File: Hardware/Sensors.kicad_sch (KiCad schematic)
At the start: 8 parts, among them U11 DPS368, U7 BU27006MUC-ZTR

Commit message: Mega commit
Post review changes
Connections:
- net CSB renamed CS_Baro
- net SDI renamed SDI_Baro
- net SDO renamed SDO_Baro
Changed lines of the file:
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@@
 		)
 	)
-	(hierarchical_label "SDO"
+	(hierarchical_label "SDO_Baro"
 		(shape output)
 		(at 119.38 85.09 180)
@@
 		)
 	)
-	(hierarchical_label "CSB"
+	(hierarchical_label "CS_Baro"
 		(shape input)
 		(at 119.38 77.47 180)
@@
 		)
 	)
-	(hierarchical_label "SDI"
+	(hierarchical_label "SDI_Baro"
 		(shape bidirectional)
 		(at 119.38 82.55 180)

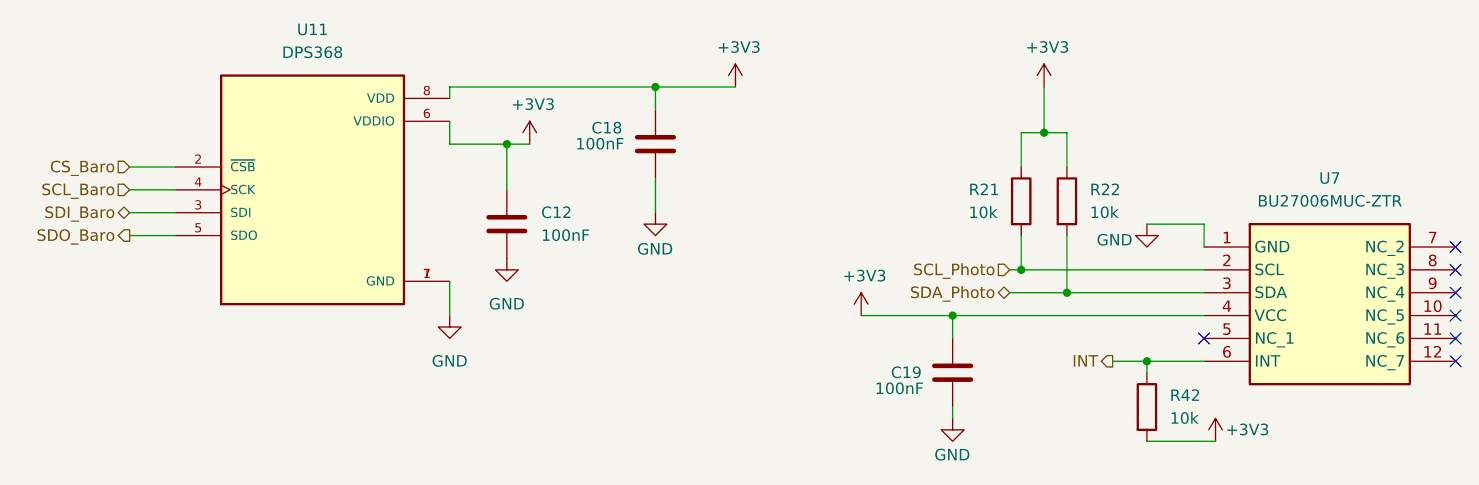
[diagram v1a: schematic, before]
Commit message: V2 hardware changes
- Removed current sensor IC
- Removed photo sensor IC
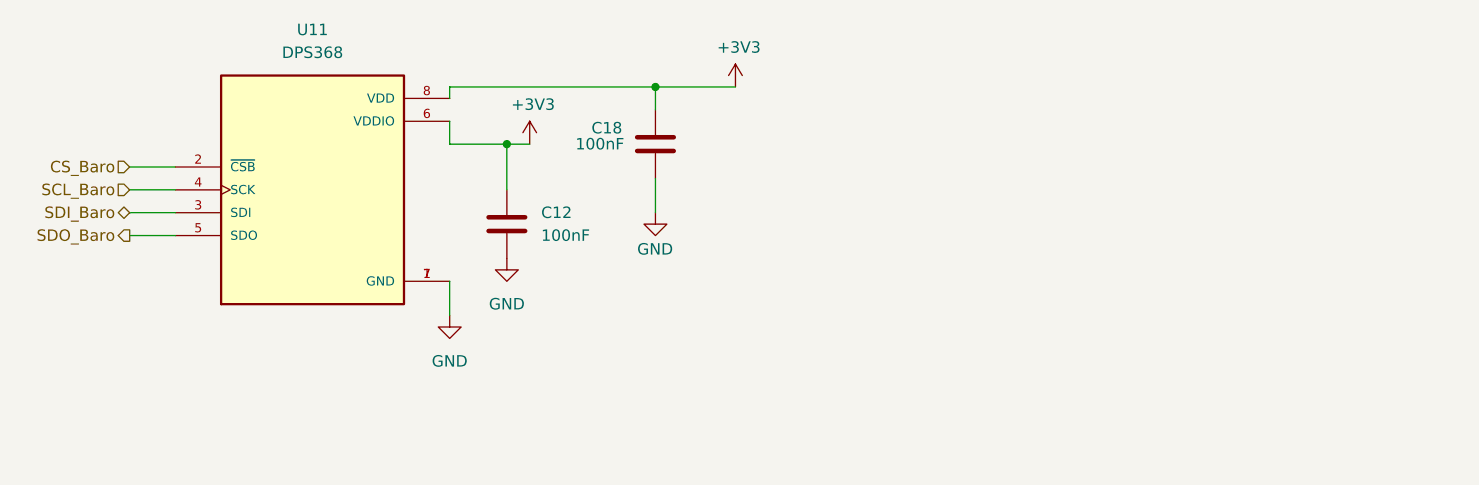
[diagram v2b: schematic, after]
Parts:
- removed C19: 100nF, Capacitor_SMD:C_0402_1005Metric, symbol Device:C
- removed R21, R22, R42: 10k, Resistor_SMD:R_0402_1005Metric, symbol Device:R
- removed U7: BU27006MUC-ZTR, iclr:BU27006MUCZTR, symbol iclr:BU27006MUC-ZTR
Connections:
- no-connect marks 7 -> 0

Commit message: reformatted and renamed file
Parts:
- renumbered C12 to C801, C18 to C802, U11 to U801
